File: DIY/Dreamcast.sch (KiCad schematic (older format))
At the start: 5 parts, among them P1 DC Ctrl slot, P2 DC Ctrl slot, P3 DC Ctrl slot, P4 DC Ctrl slot

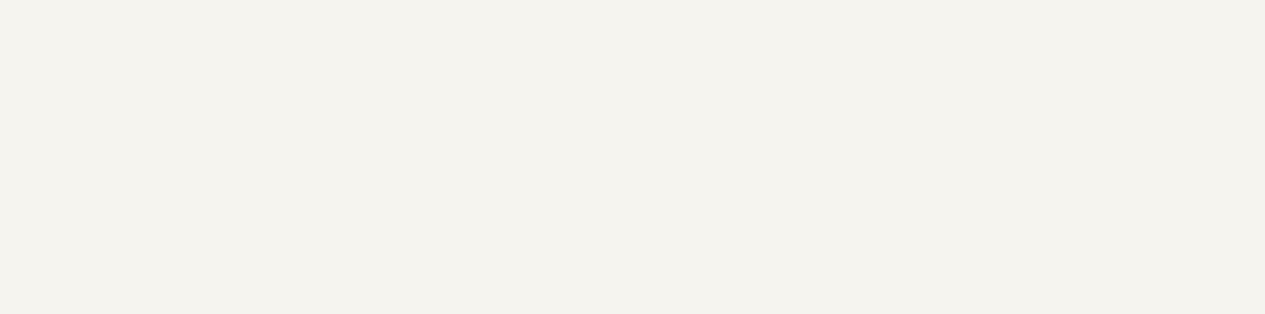
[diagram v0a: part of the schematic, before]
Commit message: [DIY] Add note to cable schematics to underline how important I39 is.
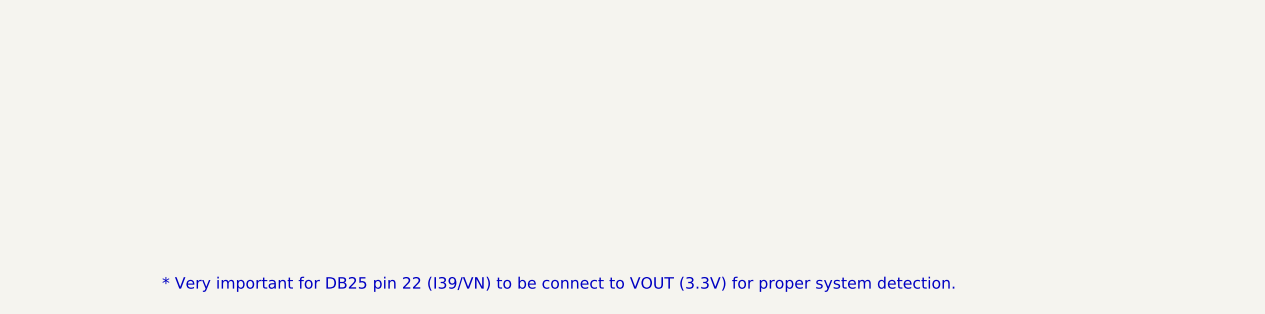
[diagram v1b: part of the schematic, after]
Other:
- note added: "* Very important for DB25 pin 22 (I39/VN) to be connect to VOUT (3.3V) for proper system detection."
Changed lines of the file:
@@
 	1    0    0    1
 $EndComp
+Text Notes 6350 6900 0    50   ~ 0
+* Very important for DB25 pin 22 (I39/VN) to be connect to VOUT (3.3V) for proper system detection.
 $EndSCHEMATC

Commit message: Use new port symbol in cable schematic
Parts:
- P1, P2, P3, P4: symbol Connector_Generic_Shielded:Conn_01x05_Shielded -> Connector_Gaming:Dreamcast
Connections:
- wire segments 79 -> 92
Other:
- note added: "Connectors facing console"

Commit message: Update adapter cable schematics
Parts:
- gave numbers to parts that had none: 1
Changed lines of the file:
@@
 $Descr USLetter 11000 8500
 encoding utf-8
-Sheet 7 7
+Sheet 7 10
 Title "BlueRetro - Dreamcast adapter cable"
 Date "2020-10-02"
@@
 P 6350 3600
 AR Path="/5F4CFDBE" Ref="#PWR?"  Part="1"
-AR Path="/5F458329/5F4CFDBE" Ref="#PWR?"  Part="1"
-F 0 "#PWR?" H 6350 3450 50  0001 C CNN
+AR Path="/5F458329/5F4CFDBE" Ref="#PWR0120"  Part="1"
+F 0 "#PWR0120" H 6350 3450 50  0001 C CNN
 F 1 "+5V" H 6365 3773 50  0000 C CNN
 F 2 "" H 6350 3600 50  0001 C CNN
@@
 P 6350 3800
 AR Path="/5F4CFDB1" Ref="#PWR?"  Part="1"
-AR Path="/5F458329/5F4CFDB1" Ref="#PWR?"  Part="1"
-F 0 "#PWR?" H 6350 3550 50  0001 C CNN
+AR Path="/5F458329/5F4CFDB1" Ref="#PWR0121"  Part="1"
+F 0 "#PWR0121" H 6350 3550 50  0001 C CNN
 F 1 "GND" H 6355 3627 50  0000 C CNN
 F 2 "" H 6350 3800 50  0001 C CNN
@@
 P 5200 3450
 AR Path="/5F4CFD8D" Ref="#PWR?"  Part="1"
-AR Path="/5F458329/5F4CFD8D" Ref="#PWR?"  Part="1"
-F 0 "#PWR?" H 5200 3200 50  0001 C CNN
+AR Path="/5F458329/5F4CFD8D" Ref="#PWR0116"  Part="1"
+F 0 "#PWR0116" H 5200 3200 50  0001 C CNN
 F 1 "GND" H 5205 3277 50  0000 C CNN
 F 2 "" H 5200 3450 50  0001 C CNN
@@
 P 5200 5050
 AR Path="/5F4CFD87" Ref="#PWR?"  Part="1"
-AR Path="/5F458329/5F4CFD87" Ref="#PWR?"  Part="1"
-F 0 "#PWR?" H 5200 4800 50  0001 C CNN
+AR Path="/5F458329/5F4CFD87" Ref="#PWR0117"  Part="1"
+F 0 "#PWR0117" H 5200 4800 50  0001 C CNN
 F 1 "GND" H 5205 4877 50  0000 C CNN
 F 2 "" H 5200 5050 50  0001 C CNN
@@
 P 3950 5050
 AR Path="/5F4CFD81" Ref="#PWR?"  Part="1"
-AR Path="/5F458329/5F4CFD81" Ref="#PWR?"  Part="1"
-F 0 "#PWR?" H 3950 4800 50  0001 C CNN
+AR Path="/5F458329/5F4CFD81" Ref="#PWR0113"  Part="1"
+F 0 "#PWR0113" H 3950 4800 50  0001 C CNN
 F 1 "GND" H 3955 4877 50  0000 C CNN
 F 2 "" H 3950 5050 50  0001 C CNN
@@
 P 3950 3450
 AR Path="/5F4CFD7B" Ref="#PWR?"  Part="1"
-AR Path="/5F458329/5F4CFD7B" Ref="#PWR?"  Part="1"
-F 0 "#PWR?" H 3950 3200 50  0001 C CNN
+AR Path="/5F458329/5F4CFD7B" Ref="#PWR0112"  Part="1"
+F 0 "#PWR0112" H 3950 3200 50  0001 C CNN
 F 1 "GND" H 3955 3277 50  0000 C CNN
 F 2 "" H 3950 3450 50  0001 C CNN
@@
 P 5300 4900
 AR Path="/5F4CFD55" Ref="#PWR?"  Part="1"
-AR Path="/5F458329/5F4CFD55" Ref="#PWR?"  Part="1"
-F 0 "#PWR?" H 5300 4750 50  0001 C CNN
+AR Path="/5F458329/5F4CFD55" Ref="#PWR0119"  Part="1"
+F 0 "#PWR0119" H 5300 4750 50  0001 C CNN
 F 1 "+5V" H 5315 5073 50  0000 C CNN
 F 2 "" H 5300 4900 50  0001 C CNN
@@
 P 5300 3300
 AR Path="/5F4CFD4F" Ref="#PWR?"  Part="1"
-AR Path="/5F458329/5F4CFD4F" Ref="#PWR?"  Part="1"
-F 0 "#PWR?" H 5300 3150 50  0001 C CNN
+AR Path="/5F458329/5F4CFD4F" Ref="#PWR0118"  Part="1"
+F 0 "#PWR0118" H 5300 3150 50  0001 C CNN
 F 1 "+5V" H 5315 3473 50  0000 C CNN
 F 2 "" H 5300 3300 50  0001 C CNN
@@
 P 4050 4900
 AR Path="/5F4CFD49" Ref="#PWR?"  Part="1"
-AR Path="/5F458329/5F4CFD49" Ref="#PWR?"  Part="1"
-F 0 "#PWR?" H 4050 4750 50  0001 C CNN
+AR Path="/5F458329/5F4CFD49" Ref="#PWR0115"  Part="1"
+F 0 "#PWR0115" H 4050 4750 50  0001 C CNN
 F 1 "+5V" H 4065 5073 50  0000 C CNN
 F 2 "" H 4050 4900 50  0001 C CNN
@@
 P 4050 3300
 AR Path="/5F4CFD43" Ref="#PWR?"  Part="1"
-AR Path="/5F458329/5F4CFD43" Ref="#PWR?"  Part="1"
-F 0 "#PWR?" H 4050 3150 50  0001 C CNN
+AR Path="/5F458329/5F4CFD43" Ref="#PWR0114"  Part="1"
+F 0 "#PWR0114" H 4050 3150 50  0001 C CNN
 F 1 "+5V" H 4065 3473 50  0000 C CNN
 F 2 "" H 4050 3300 50  0001 C CNN
@@
 P 7100 3650
 AR Path="/5F4CFD3D" Ref="J?"  Part="1"
-AR Path="/5F458329/5F4CFD3D" Ref="J?"  Part="1"
-F 0 "J?" H 7280 3696 50  0001 L CNN
+AR Path="/5F458329/5F4CFD3D" Ref="J9"  Part="1"
+F 0 "J9" H 7280 3696 50  0001 L CNN
 F 1 "DB25_Male" H 6900 2250 50  0000 L CNN
 F 2 "" H 7100 3650 50  0001 C CNN
